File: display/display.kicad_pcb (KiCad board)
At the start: 2 copper layers, 68.4 x 20.5 mm, 46 parts, among them P1 CONN_14

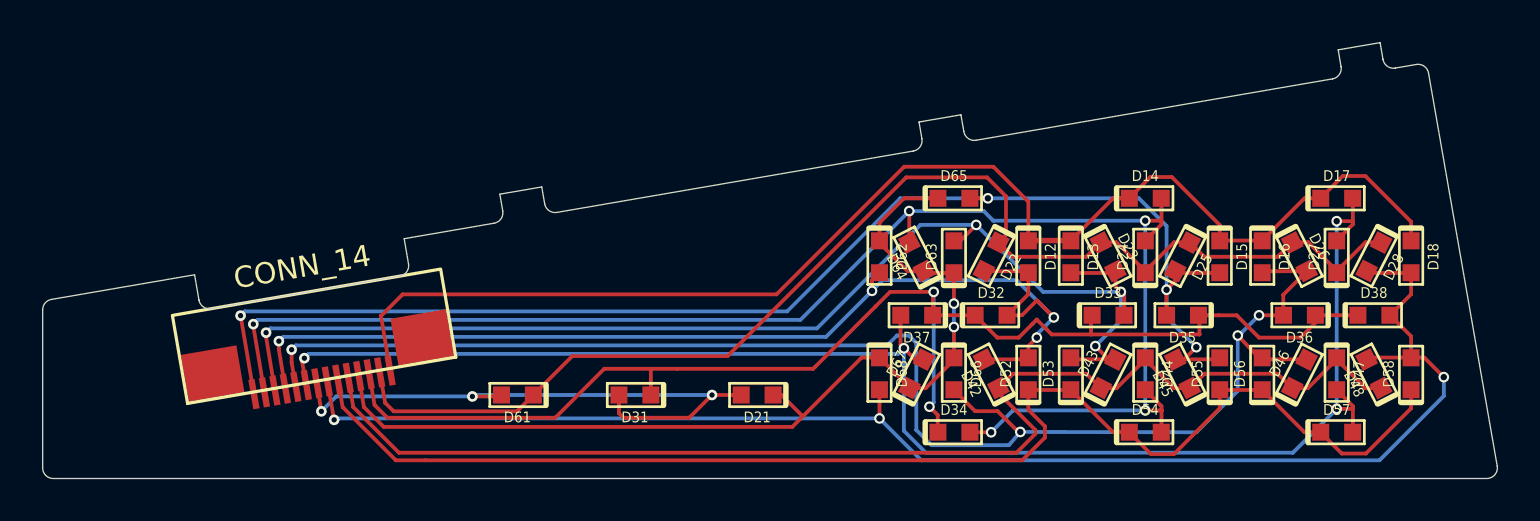
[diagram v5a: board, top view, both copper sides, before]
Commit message: Further improve routing by utilizing the available space.
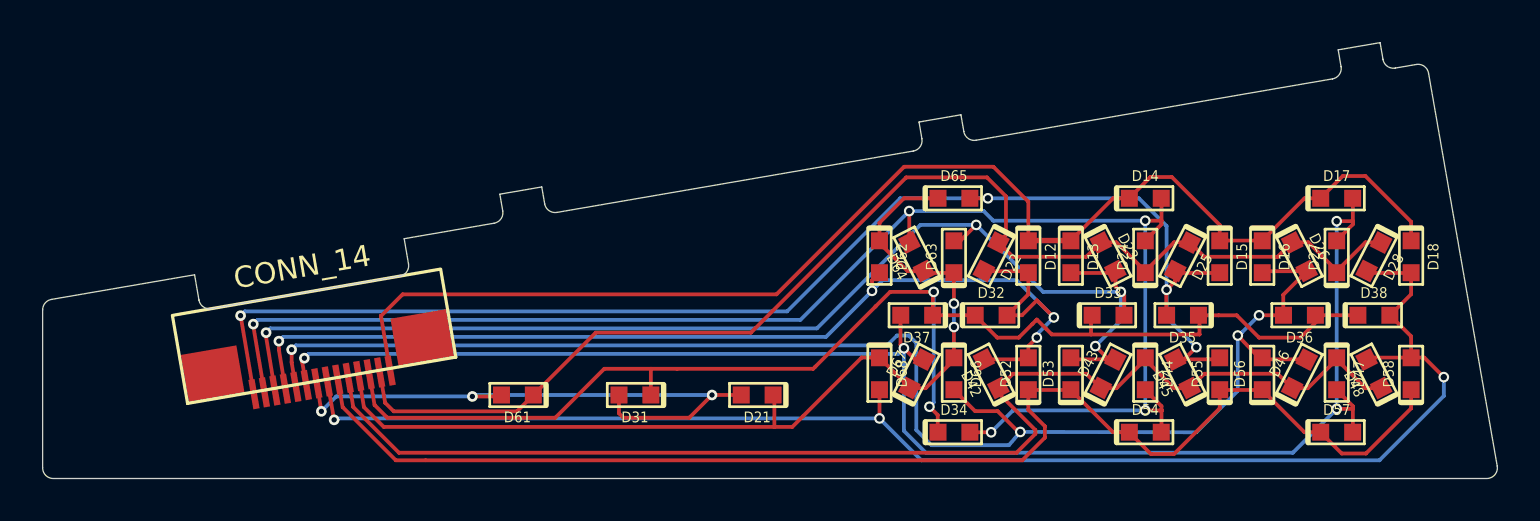
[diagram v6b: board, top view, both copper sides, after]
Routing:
- net (no net): track 57.8 -> 1.53 mm
- net /ROW2: track 18.8 -> 59.8 mm
- net /ROW1: track 45.6 -> 62.4 mm
- net /ROW4: track 46.3 -> 44.5 mm
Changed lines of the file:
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@@
     (thickness 1.6002)
     (drawings 33)
-    (tracks 379)
+    (tracks 380)
     (zones 0)
     (modules 46)
@@
   (gr_line (start 135.992156 96.388669) (end 136.127883 97.177067) (angle 90) (layer Edge.Cuts) (width 0.01))
   (gr_arc (start 135.635143 97.2619) (end 135.719962 97.754651) (angle -90.01309679) (layer Edge.Cuts) (width 0.01))
-  (segment (start 160.84296 98.58178) (end 160.84296 96.74296) (width 0.1778) (layer Front) (net 0) (status 400000))
-  (segment (start 131.419099 101.1) (end 149 101.1) (width 0.1778) (layer Front) (net 9) (status 1000000))
-  (segment (start 131.419099 101.1) (end 130.402749 102.11635) (width 0.1778) (layer Front) (net 9) (status 1000000))
-  (segment (start 155 95.1) (end 149 101.1) (width 0.1778) (layer Front) (net 0) (status 1000000))
-  (segment (start 159.2 95.1) (end 155 95.1) (width 0.1778) (layer Front) (net 0) (status 1000000))
-  (segment (start 160.84296 96.74296) (end 159.2 95.1) (width 0.1778) (layer Front) (net 0) (status 1000000))
-  (segment (start 159.7914 98.30308) (end 159.7914 96.4914) (width 0.1778) (layer Front) (net 0))
-  (segment (start 146.7 104) (end 139.39936 104) (width 0.1778) (layer Front) (net 10))
-  (segment (start 139.39936 104) (end 137.56772 105.83164) (width 0.1778) (layer Front) (net 10))
-  (segment (start 174.01032 98.6536) (end 175.34128 99.98456) (width 0.1778) (layer Front) (net 0))
-  (segment (start 175.34128 99.98456) (end 175.34128 100.09378) (width 0.1778) (layer Front) (net 0))
-  (segment (start 175.34128 100.00742) (end 176.6951 98.6536) (width 0.1778) (layer Front) (net 0))
-  (segment (start 176.6951 98.6536) (end 177.43932 98.6536) (width 0.1778) (layer Front) (net 0))
-  (segment (start 175.34128 100.09378) (end 175.34128 100.00742) (width 0.1778) (layer Front) (net 0))
-  (segment (start 164.24402 98.6536) (end 163.5633 99.33432) (width 0.1778) (layer Front) (net 0))
-  (segment (start 160.1216 99.33432) (end 159.44088 98.6536) (width 0.1778) (layer Front) (net 0))
-  (segment (start 163.5633 99.33432) (end 160.1216 99.33432) (width 0.1778) (layer Front) (net 0))
-  (segment (start 166.34206 100.09378) (end 166.34206 100.00996) (width 0.1778) (layer Front) (net 0))
-  (segment (start 164.9857 98.6536) (end 164.24402 98.6536) (width 0.1778) (layer Front) (net 0))
-  (segment (start 166.34206 100.00996) (end 164.9857 98.6536) (width 0.1778) (layer Front) (net 0))
-  (segment (start 168.4401 98.6536) (end 167.69588 98.6536) (width 0.1778) (layer Front) (net 0))
-  (segment (start 166.34206 100.00742) (end 166.34206 100.09378) (width 0.1778) (layer Front) (net 0))
-  (segment (start 167.69588 98.6536) (end 166.34206 100.00742) (width 0.1778) (layer Front) (net 0))
-  (segment (start 173.24324 98.6536) (end 172.56252 99.33432) (width 0.1778) (layer Front) (net 0))
-  (segment (start 169.12082 99.33432) (end 168.4401 98.6536) (width 0.1778) (layer Front) (net 0))
-  (segment (start 172.56252 99.33432) (end 169.12082 99.33432) (width 0.1778) (layer Front) (net 0))
-  (segment (start 173.24324 98.6536) (end 174.01032 98.6536) (width 0.1778) (layer Front) (net 0))
-  (segment (start 159.44088 98.6536) (end 159.7914 98.30308) (width 0.1778) (layer Front) (net 0))
-  (segment (start 155.1 95.6) (end 146.7 104) (width 0.1778) (layer Front) (net 0))
-  (segment (start 158.9 95.6) (end 155.1 95.6) (width 0.1778) (layer Front) (net 0))
-  (segment (start 159.7914 96.4914) (end 158.9 95.6) (width 0.1778) (layer Front) (net 0))
+  (segment (start 148.84216 105.83164) (end 148.9 105.88948) (width 0.1778) (layer Front) (net 0) (status C00000))
+  (segment (start 148.9 105.88948) (end 148.9 107.33278) (width 0.1778) (layer Front) (net 0) (status 400000))
   (segment (start 129.634 106.934) (end 128.266 106.934) (width 0.1778) (layer Back) (net 1))
   (via (at 128.2 107) (size 0.50038) (layers Front Back) (net 1))
@@
   (segment (start 169.84218 100.09378) (end 167.82796 100.09378) (width 0.1778) (layer Front) (net 8))
   (segment (start 167.82796 100.09378) (end 167.74414 100.00996) (width 0.1778) (layer Front) (net 8))
+  (segment (start 160.84296 98.58178) (end 160.84296 96.74296) (width 0.1778) (layer Front) (net 9))
+  (segment (start 131.419099 101.1) (end 149 101.1) (width 0.1778) (layer Front) (net 9))
+  (segment (start 131.419099 101.1) (end 130.402749 102.11635) (width 0.1778) (layer Front) (net 9))
+  (segment (start 155 95.1) (end 149 101.1) (width 0.1778) (layer Front) (net 9))
+  (segment (start 159.2 95.1) (end 155 95.1) (width 0.1778) (layer Front) (net 9))
+  (segment (start 160.84296 96.74296) (end 159.2 95.1) (width 0.1778) (layer Front) (net 9))
   (segment (start 130.834477 104.684073) (end 130.402749 102.11635) (width 0.1778) (layer Front) (net 9))
   (segment (start 169.84218 98.56978) (end 169.84218 97.83572) (width 0.1778) (layer Front) (net 9))
@@
   (segment (start 162.84194 98.56978) (end 160.84296 98.56978) (width 0.254) (layer Front) (net 9))
   (segment (start 130.402749 102.11635) (end 130.4 102.1) (width 0.1778) (layer Front) (net 9))
+  (segment (start 155.1 95.6) (end 147.8 102.9) (width 0.1778) (layer Front) (net 10))
+  (segment (start 159.7914 96.4914) (end 158.9 95.6) (width 0.1778) (layer Front) (net 10))
+  (segment (start 158.9 95.6) (end 155.1 95.6) (width 0.1778) (layer Front) (net 10))
+  (segment (start 159.44088 98.6536) (end 159.7914 98.30308) (width 0.1778) (layer Front) (net 10))
+  (segment (start 173.24324 98.6536) (end 174.01032 98.6536) (width 0.1778) (layer Front) (net 10))
+  (segment (start 172.56252 99.33432) (end 169.12082 99.33432) (width 0.1778) (layer Front) (net 10))
+  (segment (start 169.12082 99.33432) (end 168.4401 98.6536) (width 0.1778) (layer Front) (net 10))
+  (segment (start 173.24324 98.6536) (end 172.56252 99.33432) (width 0.1778) (layer Front) (net 10))
+  (segment (start 167.69588 98.6536) (end 166.34206 100.00742) (width 0.1778) (layer Front) (net 10))
+  (segment (start 166.34206 100.00742) (end 166.34206 100.09378) (width 0.1778) (layer Front) (net 10))
+  (segment (start 168.4401 98.6536) (end 167.69588 98.6536) (width 0.1778) (layer Front) (net 10))
+  (segment (start 166.34206 100.00996) (end 164.9857 98.6536) (width 0.1778) (layer Front) (net 10))
+  (segment (start 164.9857 98.6536) (end 164.24402 98.6536) (width 0.1778) (layer Front) (net 10))
+  (segment (start 166.34206 100.09378) (end 166.34206 100.00996) (width 0.1778) (layer Front) (net 10))
+  (segment (start 163.5633 99.33432) (end 160.1216 99.33432) (width 0.1778) (layer Front) (net 10))
+  (segment (start 160.1216 99.33432) (end 159.44088 98.6536) (width 0.1778) (layer Front) (net 10))
+  (segment (start 164.24402 98.6536) (end 163.5633 99.33432) (width 0.1778) (layer Front) (net 10))
+  (segment (start 175.34128 100.09378) (end 175.34128 100.00742) (width 0.1778) (layer Front) (net 10))
+  (segment (start 177.43932 98.6536) (end 176.6951 98.6536) (width 0.1778) (layer Front) (net 10))
+  (segment (start 175.34128 100.00742) (end 176.6951 98.6536) (width 0.1778) (layer Front) (net 10))
+  (segment (start 175.34128 99.98456) (end 175.34128 100.09378) (width 0.1778) (layer Front) (net 10))
+  (segment (start 174.01032 98.6536) (end 175.34128 99.98456) (width 0.1778) (layer Front) (net 10))
+  (segment (start 159.7914 98.30308) (end 159.7914 96.4914) (width 0.1778) (layer Front) (net 10))
+  (segment (start 140.49936 102.9) (end 137.56772 105.83164) (width 0.1778) (layer Front) (net 10) (status 800000))
+  (segment (start 147.8 102.9) (end 140.49936 102.9) (width 0.1778) (layer Front) (net 10))
   (segment (start 130.6 106.2) (end 131 106.6) (width 0.1778) (layer Front) (net 10))
   (segment (start 137.56772 105.83164) (end 136.79936 106.6) (width 0.1778) (layer Front) (net 10))
@@
   (segment (start 157.34284 101.53396) (end 157.34284 102.63378) (width 0.1778) (layer Back) (net 12))
   (via (at 157.34284 101.53396) (size 0.50038) (drill 0.29972) (layers Front Back) (net 12))
-  (segment (start 148.84216 105.83164) (end 149.23164 105.83164) (width 0.1778) (layer Front) (net 12))
-  (segment (start 149.23164 105.83164) (end 150.23797 106.83797) (width 0.1778) (layer Front) (net 12))
-  (segment (start 130.53278 107.33278) (end 149.74316 107.33278) (width 0.1778) (layer Front) (net 12))
+  (segment (start 130.53278 107.33278) (end 148.9 107.33278) (width 0.1778) (layer Front) (net 12))
+  (segment (start 148.9 107.33278) (end 149.74316 107.33278) (width 0.1778) (layer Front) (net 12))
   (segment (start 129.6 106.4) (end 130.53278 107.33278) (width 0.1778) (layer Front) (net 12))
   (segment (start 129.356365 104.939387) (end 129.6 106.4) (width 0.1778) (layer Front) (net 12))

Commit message: Again, utilize the available space better.
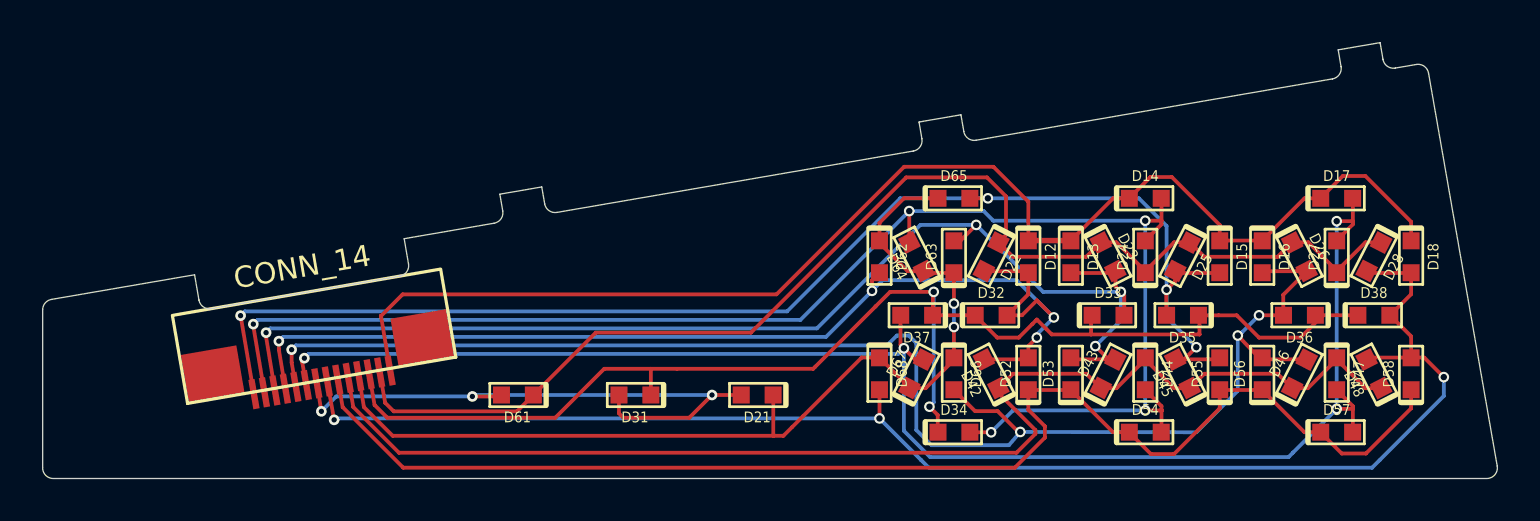
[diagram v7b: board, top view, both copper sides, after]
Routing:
- net /ROW4: track 44.5 -> 46.7 mm
- net (no net): track 1.53 -> 0.00 mm

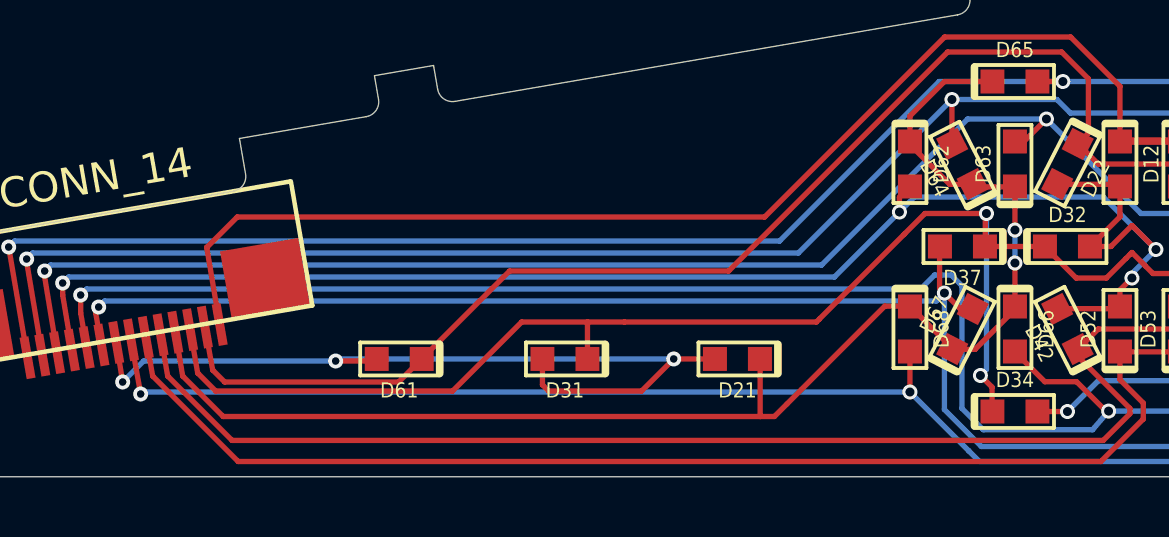
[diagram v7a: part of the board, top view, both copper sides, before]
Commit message: Further optimize routing.
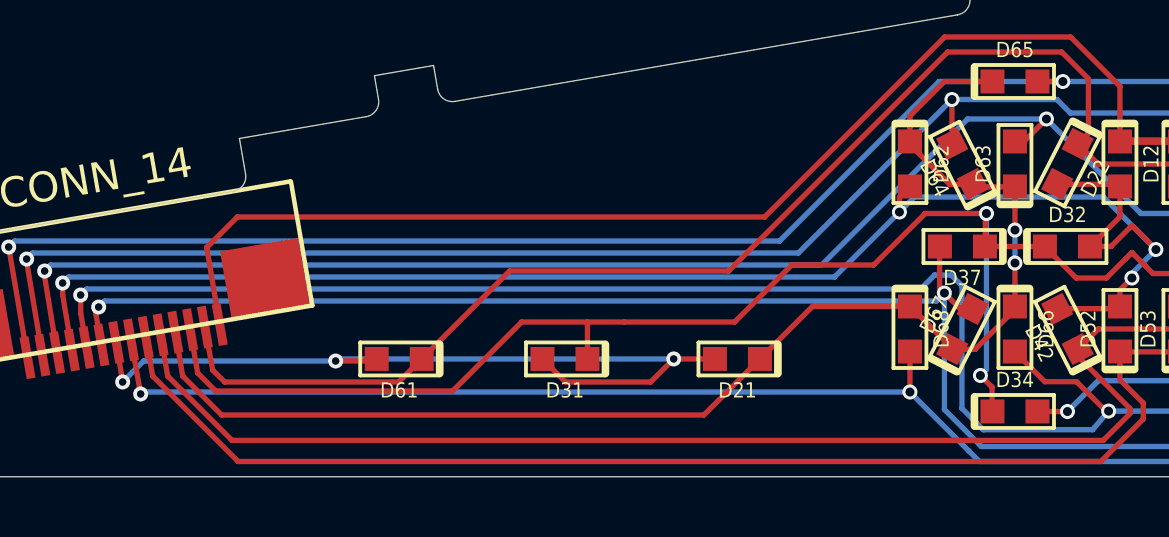
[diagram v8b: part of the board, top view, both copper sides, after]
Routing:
- net /COL2: track 28.6 -> 22.8 mm
- net (no net): track 0.00 -> 5.01 mm
- net /ROW4: track 46.7 -> 44.8 mm
